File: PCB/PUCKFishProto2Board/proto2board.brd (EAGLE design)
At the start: 160 x 100 mm, 10 parts, among them U1 MS583730BA01-50, U2 ZXCT1107SA-7

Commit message: Schematic done except salinity sensor
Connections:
- removed net +3V3: JP2.15
- removed net 3.3V: JP3.2, JP6.2
- removed net AD0: JP5.1
- removed net ADDR: JP3.6
- removed net CLKIN: JP5.5
- removed net FSYNC_IN: JP5.2
- removed net INT: JP6.6
- removed net SCL_EXT: JP5.3
- removed net SDA_EXT: JP5.4
- removed net VDD: U1.2
- net GND: no longer JP5.6
- net SCL: now also U1.3
- net SDA: now also U1.4
- net VCC: now also JP2.15, U1.2
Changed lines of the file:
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@@
 </elements>
 <signals>
-<signal name="VDD">
-<contactref element="U1" pad="2"/>
-</signal>
 <signal name="GND" class="1">
-<contactref element="U1" pad="1"/>
 <polygon width="0.254" layer="1">
 <vertex x="160.02" y="76.2"/>
@@
 </polygon>
 <contactref element="JP2" pad="13"/>
-<contactref element="JP5" pad="6"/>
 <contactref element="JP6" pad="3"/>
 <polygon width="0.254" layer="1">
@@
 <vertex x="134.62" y="33.02"/>
 </polygon>
-<wire x1="153.67" y1="69.85" x2="146.05" y2="97.79" width="0" layer="19" extent="1-1"/>
-<wire x1="146.05" y1="57.15" x2="153.67" y2="69.85" width="0" layer="19" extent="1-1"/>
+<contactref element="U1" pad="1"/>
+<wire x1="146.05" y1="57.15" x2="146.05" y2="97.79" width="0" layer="19" extent="1-1"/>
 <wire x1="146.05" y1="35.56" x2="146.05" y2="57.15" width="0" layer="19" extent="1-1"/>
-<wire x1="108.22" y1="53.07" x2="146.05" y2="35.56" width="0" layer="19" extent="1-1"/>
+<wire x1="108.22" y1="53.07" x2="146.05" y2="57.15" width="0" layer="19" extent="1-1"/>
 </signal>
 <signal name="MOSI">
@@
 <contactref element="JP4" pad="5"/>
 </signal>
-<signal name="+3V3">
-<contactref element="JP2" pad="15"/>
-</signal>
 <signal name="VBUS">
 <contactref element="JP4" pad="3"/>
@@
 <contactref element="JP6" pad="4"/>
 <contactref element="JP3" pad="4"/>
+<contactref element="U1" pad="3"/>
 <wire x1="148.59" y1="35.56" x2="148.59" y2="57.15" width="0" layer="19" extent="1-1"/>
 <wire x1="118.11" y1="77.47" x2="148.59" y2="57.15" width="0" layer="19" extent="1-1"/>
+<wire x1="110.22" y1="51.07" x2="118.11" y2="77.47" width="0" layer="19" extent="1-1"/>
 </signal>
 <signal name="SDA">
@@
 <contactref element="JP6" pad="5"/>
 <contactref element="JP3" pad="5"/>
+<contactref element="U1" pad="4"/>
 <wire x1="151.13" y1="35.56" x2="151.13" y2="57.15" width="0" layer="19" extent="1-1"/>
 <wire x1="115.57" y1="77.47" x2="151.13" y2="57.15" width="0" layer="19" extent="1-1"/>
+<wire x1="110.22" y1="53.07" x2="115.57" y2="77.47" width="0" layer="19" extent="1-1"/>
 </signal>
 <signal name="D9">
@@
 <contactref element="JP2" pad="1"/>
 </signal>
-<signal name="3.3V">
-<contactref element="JP6" pad="2"/>
-<contactref element="JP3" pad="2"/>
-<wire x1="143.51" y1="35.56" x2="143.51" y2="57.15" width="0" layer="19" extent="1-1"/>
-</signal>
-<signal name="FSYNC_IN">
-<contactref element="JP5" pad="2"/>
-</signal>
-<signal name="CLKIN">
-<contactref element="JP5" pad="5"/>
-</signal>
-<signal name="SDA_EXT">
-<contactref element="JP5" pad="4"/>
-</signal>
-<signal name="SCL_EXT">
-<contactref element="JP5" pad="3"/>
-</signal>
-<signal name="AD0">
-<contactref element="JP5" pad="1"/>
-</signal>
-<signal name="INT">
-<contactref element="JP6" pad="6"/>
-</signal>
 <signal name="VCC" class="1">
 <contactref element="JP6" pad="1"/>
 <contactref element="JP3" pad="1"/>
+<contactref element="JP2" pad="15"/>
+<contactref element="U1" pad="2"/>
+<wire x1="140.97" y1="57.15" x2="151.13" y2="97.79" width="0" layer="19" extent="1-1"/>
 <wire x1="140.97" y1="35.56" x2="140.97" y2="57.15" width="0" layer="19" extent="1-1"/>
-</signal>
-<signal name="ADDR">
-<contactref element="JP3" pad="6"/>
+<wire x1="108.22" y1="51.07" x2="140.97" y2="57.15" width="0" layer="19" extent="1-1"/>
 </signal>
 </signals>

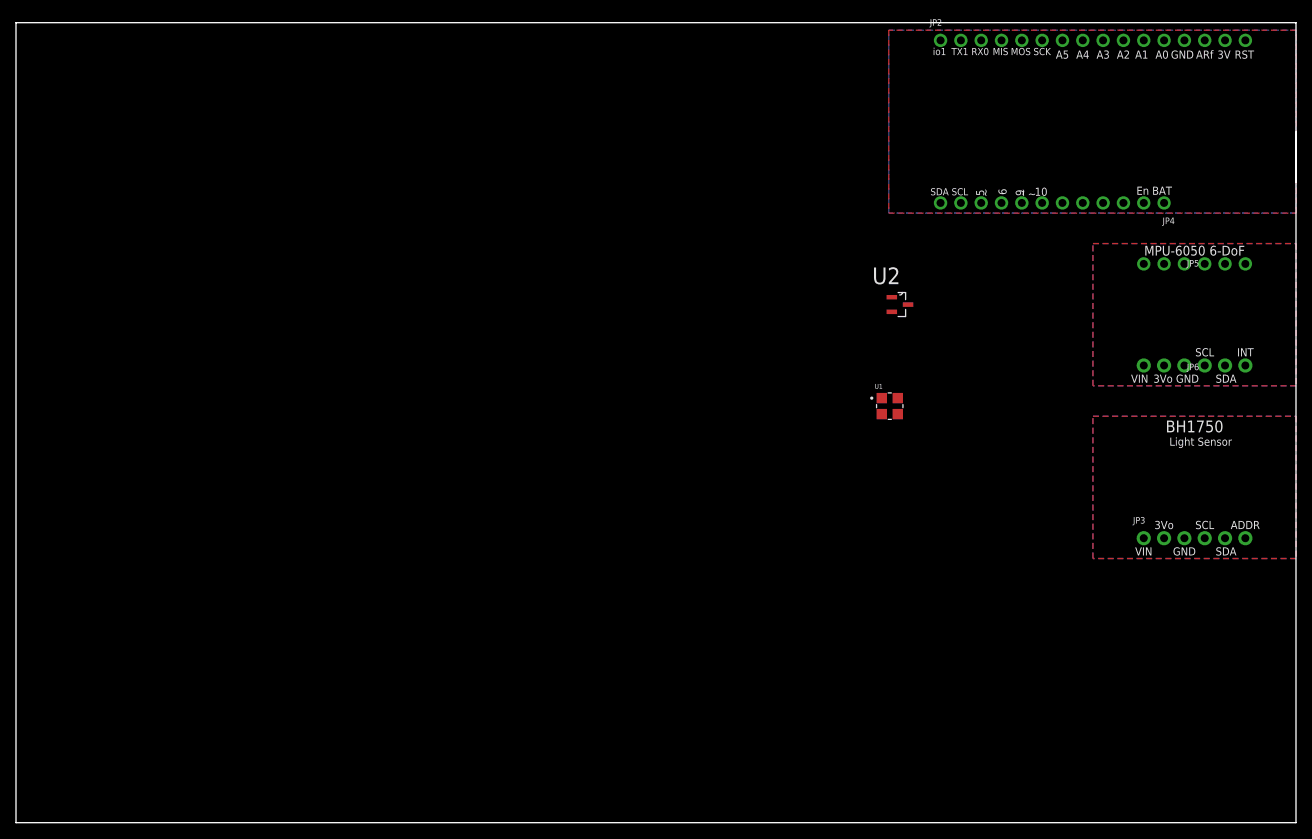
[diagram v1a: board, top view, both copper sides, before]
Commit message: Reduced board size
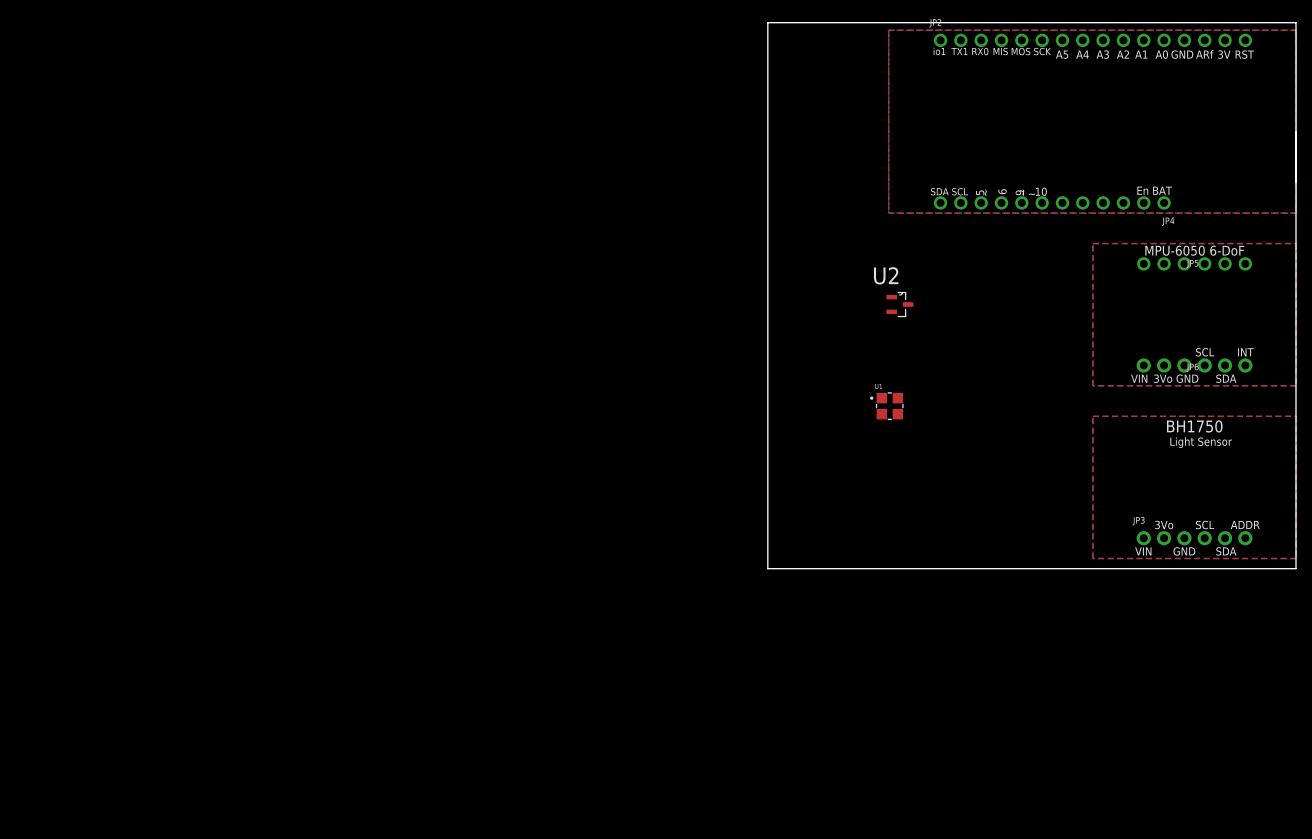
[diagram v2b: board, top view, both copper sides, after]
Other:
- board size 160 x 100 mm -> 66 x 68.2 mm
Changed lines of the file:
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@@
 <board>
 <plain>
-<wire x1="0" y1="0" x2="160" y2="0" width="0" layer="20"/>
-<wire x1="160" y1="0" x2="160" y2="100" width="0" layer="20"/>
-<wire x1="160" y1="100" x2="0" y2="100" width="0" layer="20"/>
-<wire x1="0" y1="100" x2="0" y2="0" width="0" layer="20"/>
+<wire x1="93.98" y1="31.75" x2="160" y2="31.75" width="0" layer="20"/>
+<wire x1="160" y1="31.75" x2="160" y2="100" width="0" layer="20"/>
+<wire x1="160" y1="100" x2="93.98" y2="100" width="0" layer="20"/>
+<wire x1="93.98" y1="100" x2="93.98" y2="31.75" width="0" layer="20"/>
 <wire x1="160.02" y1="80.01" x2="160.02" y2="86.36" width="0" layer="20"/>
 <text x="153.543" y="96.012" size="1.016" layer="21" ratio="12" align="center">RST</text>
@@
 <text x="147.32" y="48.26" size="1.651" layer="22" font="vector" ratio="15" rot="MR0" align="center">BH1750</text>
 <text x="147.193" y="33.909" size="1.016" layer="22" font="vector" ratio="12" rot="MR0" align="center">VLogic/Vcc: 3-5VDC</text>
+<dimension x1="93.98" y1="30.48" x2="160.02" y2="30.48" x3="127" y3="26.67" textsize="1.778" layer="1"/>
+<dimension x1="93.98" y1="31.75" x2="93.98" y2="100" x3="90.17" y3="65.875" textsize="1.778" layer="1"/>
 </plain>
 <attributes>

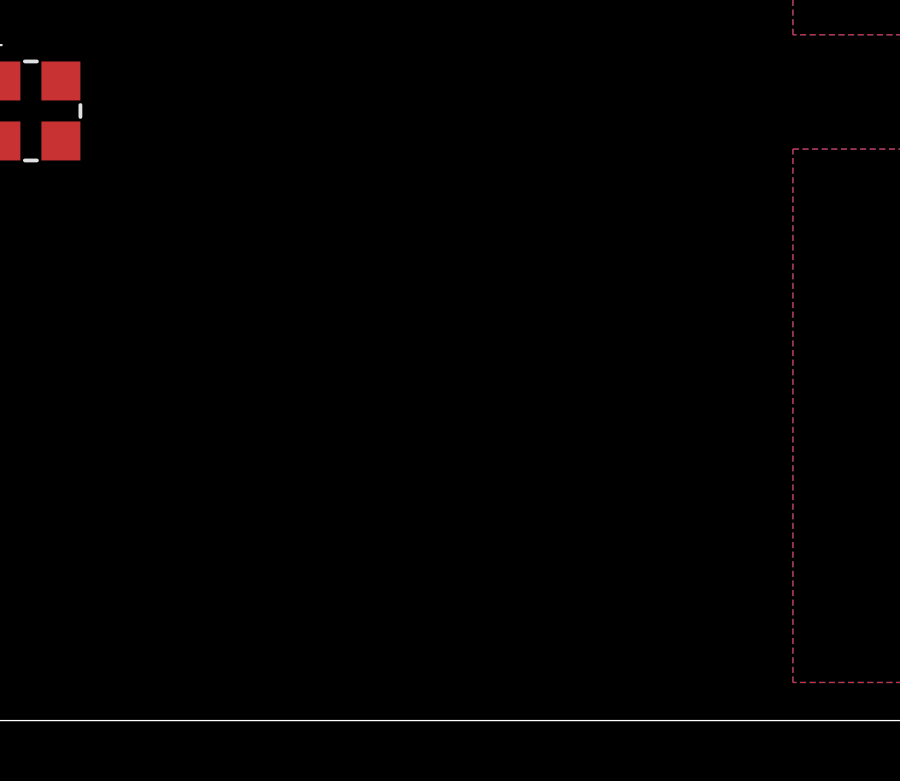
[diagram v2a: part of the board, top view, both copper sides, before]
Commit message: Salinity incorporated into sch better now
Resistors added, needs proofreading
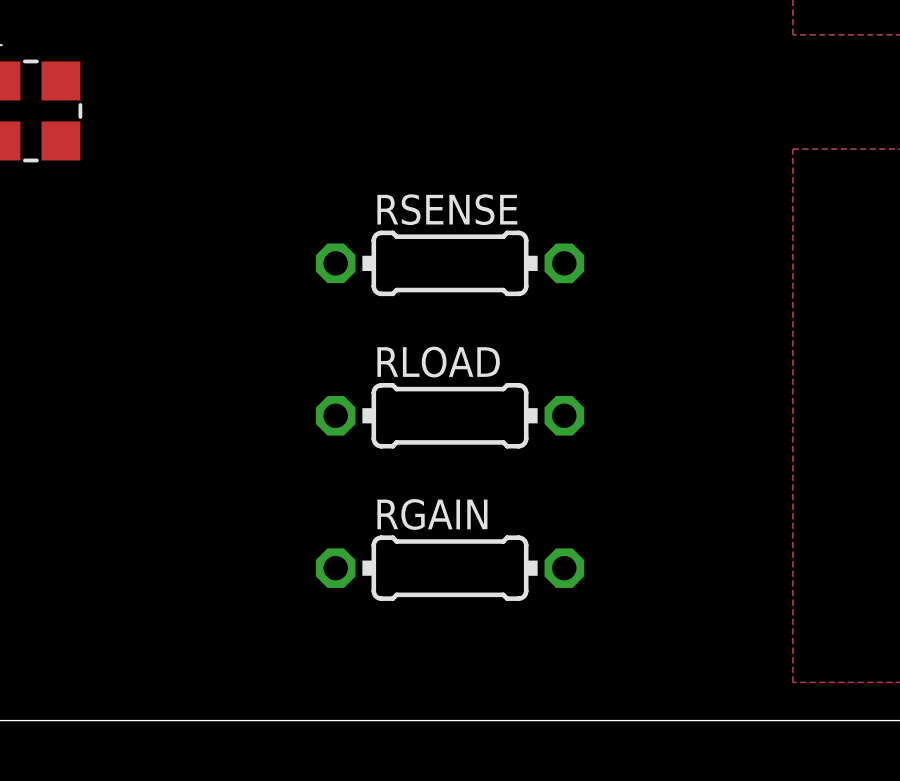
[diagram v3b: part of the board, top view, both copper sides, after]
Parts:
- added RGAIN, RLOAD, RSENSE: (no value), rcl:0204/7
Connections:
- new net N$2: RLOAD.2, RSENSE.1, U2.2
- net A0: now also RGAIN.1, U2.1
- net GND: now also RGAIN.2, RLOAD.1
- net VCC: now also RSENSE.2, U2.3
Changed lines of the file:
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@@
 <attribute name="VALUE" x="139.7" y="33.655" size="0.4064" layer="27" ratio="10"/>
+</element>
+<element name="RSENSE" library="rcl" library_urn="urn:adsk.eagle:library:334" package="0204/7" package3d_urn="urn:adsk.eagle:package:23498/2" value="" x="123.19" y="46.99" smashed="yes">
+<attribute name="NAME" x="120.65" y="48.2854" size="0.9906" layer="25" ratio="10"/>
+<attribute name="POPULARITY" value="48" x="123.19" y="46.99" size="1.778" layer="27" display="off"/>
+<attribute name="SPICEPREFIX" value="R" x="123.19" y="46.99" size="1.778" layer="27" display="off"/>
+<attribute name="VALUE" x="121.5644" y="46.5074" size="0.9906" layer="27" ratio="10"/>
+</element>
+<element name="RLOAD" library="rcl" library_urn="urn:adsk.eagle:library:334" package="0204/7" package3d_urn="urn:adsk.eagle:package:23498/2" value="" x="123.19" y="41.91" smashed="yes">
+<attribute name="NAME" x="120.65" y="43.2054" size="0.9906" layer="25" ratio="10"/>
+<attribute name="POPULARITY" value="48" x="123.19" y="41.91" size="1.778" layer="27" display="off"/>
+<attribute name="SPICEPREFIX" value="R" x="123.19" y="41.91" size="1.778" layer="27" display="off"/>
+<attribute name="VALUE" x="121.5644" y="41.4274" size="0.9906" layer="27" ratio="10"/>
+</element>
+<element name="RGAIN" library="rcl" library_urn="urn:adsk.eagle:library:334" package="0204/7" package3d_urn="urn:adsk.eagle:package:23498/2" value="" x="123.19" y="36.83" smashed="yes">
+<attribute name="NAME" x="120.65" y="38.1254" size="0.9906" layer="25" ratio="10"/>
+<attribute name="POPULARITY" value="48" x="123.19" y="36.83" size="1.778" layer="27" display="off"/>
+<attribute name="SPICEPREFIX" value="R" x="123.19" y="36.83" size="1.778" layer="27" display="off"/>
+<attribute name="VALUE" x="121.5644" y="36.3474" size="0.9906" layer="27" ratio="10"/>
 </element>
 </elements>
@@
 </polygon>
 <contactref element="U1" pad="1"/>
+<contactref element="RLOAD" pad="1"/>
+<contactref element="RGAIN" pad="2"/>
 <wire x1="146.05" y1="57.15" x2="146.05" y2="97.79" width="0" layer="19" extent="1-1"/>
 <wire x1="146.05" y1="35.56" x2="146.05" y2="57.15" width="0" layer="19" extent="1-1"/>
 <wire x1="108.22" y1="53.07" x2="146.05" y2="57.15" width="0" layer="19" extent="1-1"/>
+<wire x1="119.38" y1="41.91" x2="108.22" y2="53.07" width="0" layer="19" extent="1-1"/>
+<wire x1="127" y1="36.83" x2="119.38" y2="41.91" width="0" layer="19" extent="1-1"/>
 </signal>
 <signal name="MOSI">
@@
 <signal name="A0">
 <contactref element="JP2" pad="12"/>
+<contactref element="U2" pad="1"/>
+<contactref element="RGAIN" pad="1"/>
+<wire x1="109.474" y1="65.6844" x2="143.51" y2="97.79" width="0" layer="19" extent="1-1"/>
+<wire x1="119.38" y1="36.83" x2="109.474" y2="65.6844" width="0" layer="19" extent="1-1"/>
 </signal>
 <signal name="PB22/I6/SERCOM5.1">
@@
 <contactref element="JP2" pad="15"/>
 <contactref element="U1" pad="2"/>
+<contactref element="U2" pad="3"/>
+<contactref element="RSENSE" pad="2"/>
 <wire x1="140.97" y1="57.15" x2="151.13" y2="97.79" width="0" layer="19" extent="1-1"/>
 <wire x1="140.97" y1="35.56" x2="140.97" y2="57.15" width="0" layer="19" extent="1-1"/>
-<wire x1="108.22" y1="51.07" x2="140.97" y2="57.15" width="0" layer="19" extent="1-1"/>
+<wire x1="111.506" y1="64.77" x2="140.97" y2="57.15" width="0" layer="19" extent="1-1"/>
+<wire x1="108.22" y1="51.07" x2="111.506" y2="64.77" width="0" layer="19" extent="1-1"/>
+<wire x1="127" y1="46.99" x2="108.22" y2="51.07" width="0" layer="19" extent="1-1"/>
+</signal>
+<signal name="N$2">
+<contactref element="RSENSE" pad="1"/>
+<contactref element="U2" pad="2"/>
+<contactref element="RLOAD" pad="2"/>
+<wire x1="119.38" y1="46.99" x2="109.474" y2="63.8556" width="0" layer="19" extent="1-1"/>
+<wire x1="127" y1="41.91" x2="119.38" y2="46.99" width="0" layer="19" extent="1-1"/>
 </signal>
 </signals>
@@
 which will not be processed correctly with this version.
 </note>
+<note version="8.2" severity="warning">
+Since Version 8.2, EAGLE supports online libraries. The ids
+of those online libraries will not be understood (or retained)
+with this version.
+</note>
+<note version="8.3" severity="warning">
+Since Version 8.3, EAGLE supports URNs for individual library
+assets (packages, symbols, and devices). The URNs of those assets
+will not be understood (or retained) with this version.
+</note>
+<note version="8.3" severity="warning">
+Since Version 8.3, EAGLE supports the association of 3D packages
+with devices in libraries, schematics, and board files. Those 3D
+packages will not be understood (or retained) with this version.
+</note>
 </compatibility>

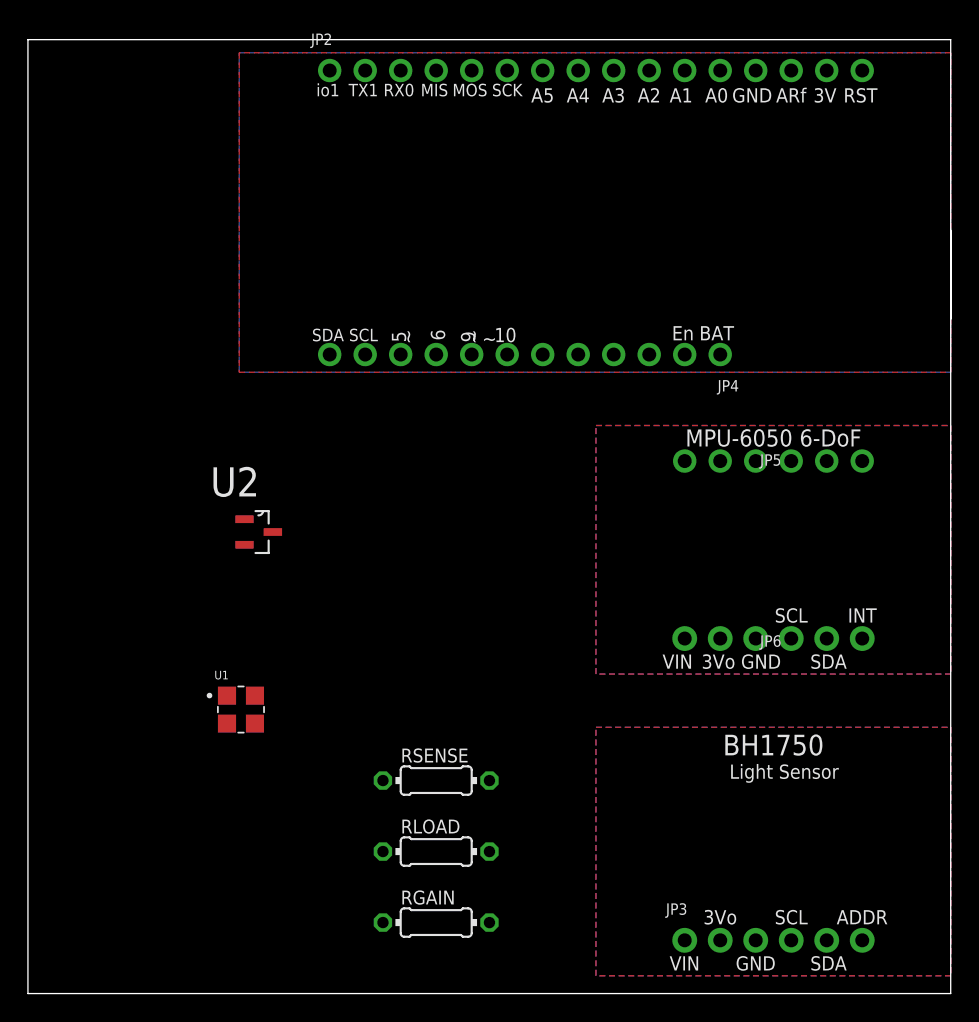
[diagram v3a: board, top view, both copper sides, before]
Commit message: PCB Layout editing
Vialess layout, exported in the zip file and being sent to JLC now
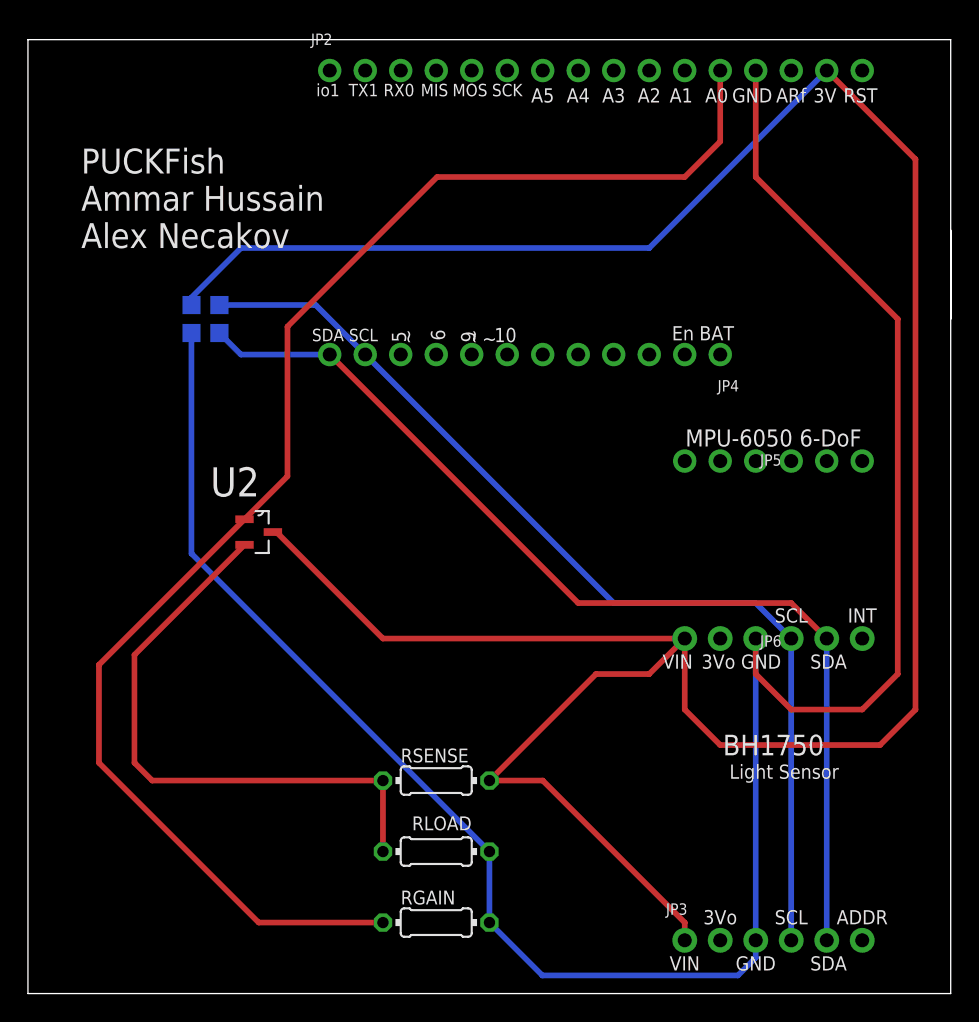
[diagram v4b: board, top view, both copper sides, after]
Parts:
- removed U$7, U$8: (no value), silks:STEMMAQT
- moved U1 28.1 mm to (106.7, 80.0), flipped to the bottom, turned to 180 degrees
- turned RLOAD to 180 degrees
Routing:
- net VCC: track 0.00 -> 195.0 mm
- net GND: track 0.00 -> 157.7 mm
- net A0: track 0.00 -> 103.4 mm
- net SDA: track 0.00 -> 74.1 mm
- net SCL: track 0.00 -> 72.4 mm
- net N$2: track 0.00 -> 42.2 mm
- removed copper zone on layer 1, net GND
- removed copper zone on layer 16, net GND
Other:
- board text added: "PUCKFish Ammar Hussain Alex Necakov"
